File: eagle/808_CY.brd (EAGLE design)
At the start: 100.8 x 82 mm, 111 parts, among them IC1 TL071P, IC2 TL072P, IC4 TL072P, Q1 2N3904, Q2 2N3904, Q3 2N3904, Q4 2N3904, Q5 2N3904, Q6 2N3904, Q7 2N3904, Q8 2N3906

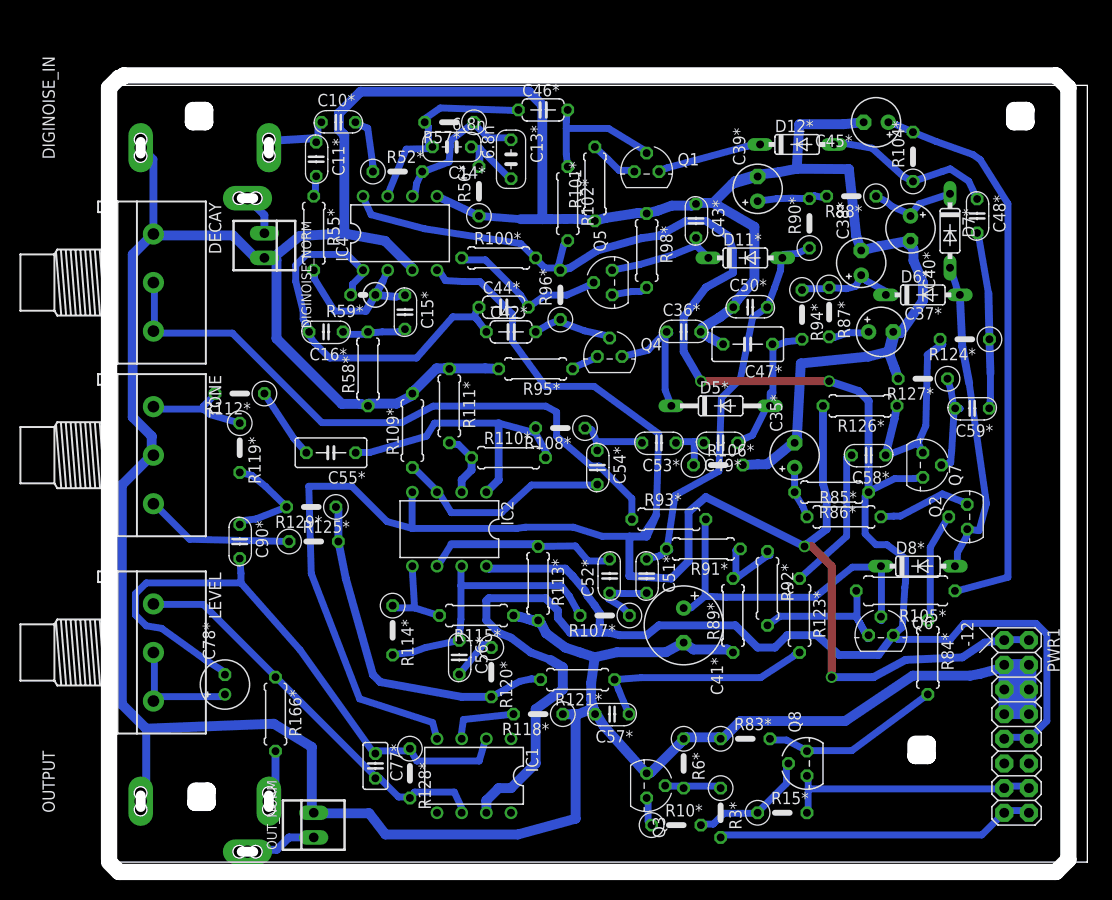
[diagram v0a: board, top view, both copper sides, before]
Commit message: will try gcode
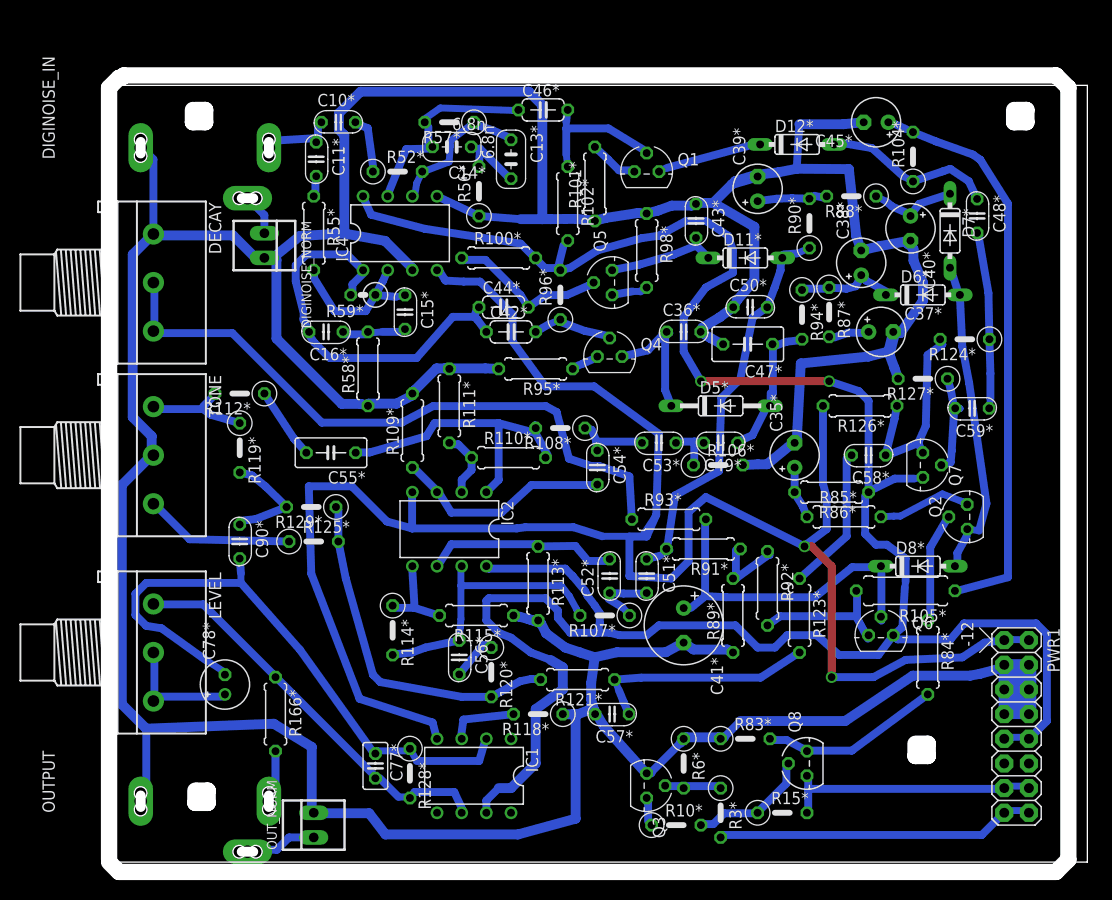
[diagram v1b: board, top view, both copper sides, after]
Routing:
- net N$178: track 66.0 -> 67.1 mm

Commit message: tweaks aftrer working build
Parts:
- C78*: device TR808clone:E2-5 -> TR808clone:E3,5-8
- moved R112* 6.75 mm to (15.0, 41.9), turned to 90 degrees
- moved C78* 5.08 mm to (11.2, 23.4)
- moved Q7 2.54 mm to (85.1, 35.6), turned to 180 degrees
- moved R119* 1.93 mm to (10.9, 41.9)
- moved R57* 1.93 mm to (32.5, 75.4)
- moved R95* 1.78 mm to (41.4, 50.8)
- moved C13* 1.55 mm to (40.9, 70.9)
- moved R55* 1.27 mm to (20.3, 63.5)
- moved R109* 1.05 mm to (29.5, 44.2)
- moved C57* 0.92 mm to (51.6, 14.5), turned to 270 degrees
- moved C44* 0.76 mm to (40.6, 57.1)
- moved R90* 0.72 mm to (70.9, 65.3), turned to 180 degrees
- moved C49* 0.51 mm to (62.2, 43.7)
- moved C14* 0.51 mm to (34.5, 73.2)
- moved R106* 0.25 mm to (62.0, 41.1)
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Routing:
- net N$544: track 64.1 -> 42.8 mm
- net N$512: track 9.69 -> 5.11 mm
- net GND: track 487.1 -> 482.7 mm
- net N$223: track 41.0 -> 43.4 mm
- net -15V: track 200.7 -> 198.4 mm
- net N$501: track 7.90 -> 10.1 mm
- net N$536: track 7.48 -> 5.36 mm
- net N$514: track 11.3 -> 9.35 mm
- net N$171: track 12.9 -> 14.8 mm
- net N$495: track 2.42 -> 4.17 mm
- net N$531: track 22.4 -> 24.1 mm
- net N$504: track 22.0 -> 23.7 mm
- net N$546: track 42.4 -> 44.2 mm
- net N$523: track 16.7 -> 15.0 mm
- net +15V: track 240.1 -> 241.8 mm
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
